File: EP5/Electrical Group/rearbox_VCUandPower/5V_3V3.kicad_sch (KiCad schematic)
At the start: 54 parts, among them IC2 LMR14050SDDAR, IC3 MCP6C04T-100E_CHY, IC4 LD39100PU33RY, J12 5V external, J13 USBC_RPI_5VOnly, J14 USBA_RPI_5Vonly, J15 fan1, J16 fan2, J17 UPS_cap, J18 5Vout, J19 Rpi, J21 3V3out

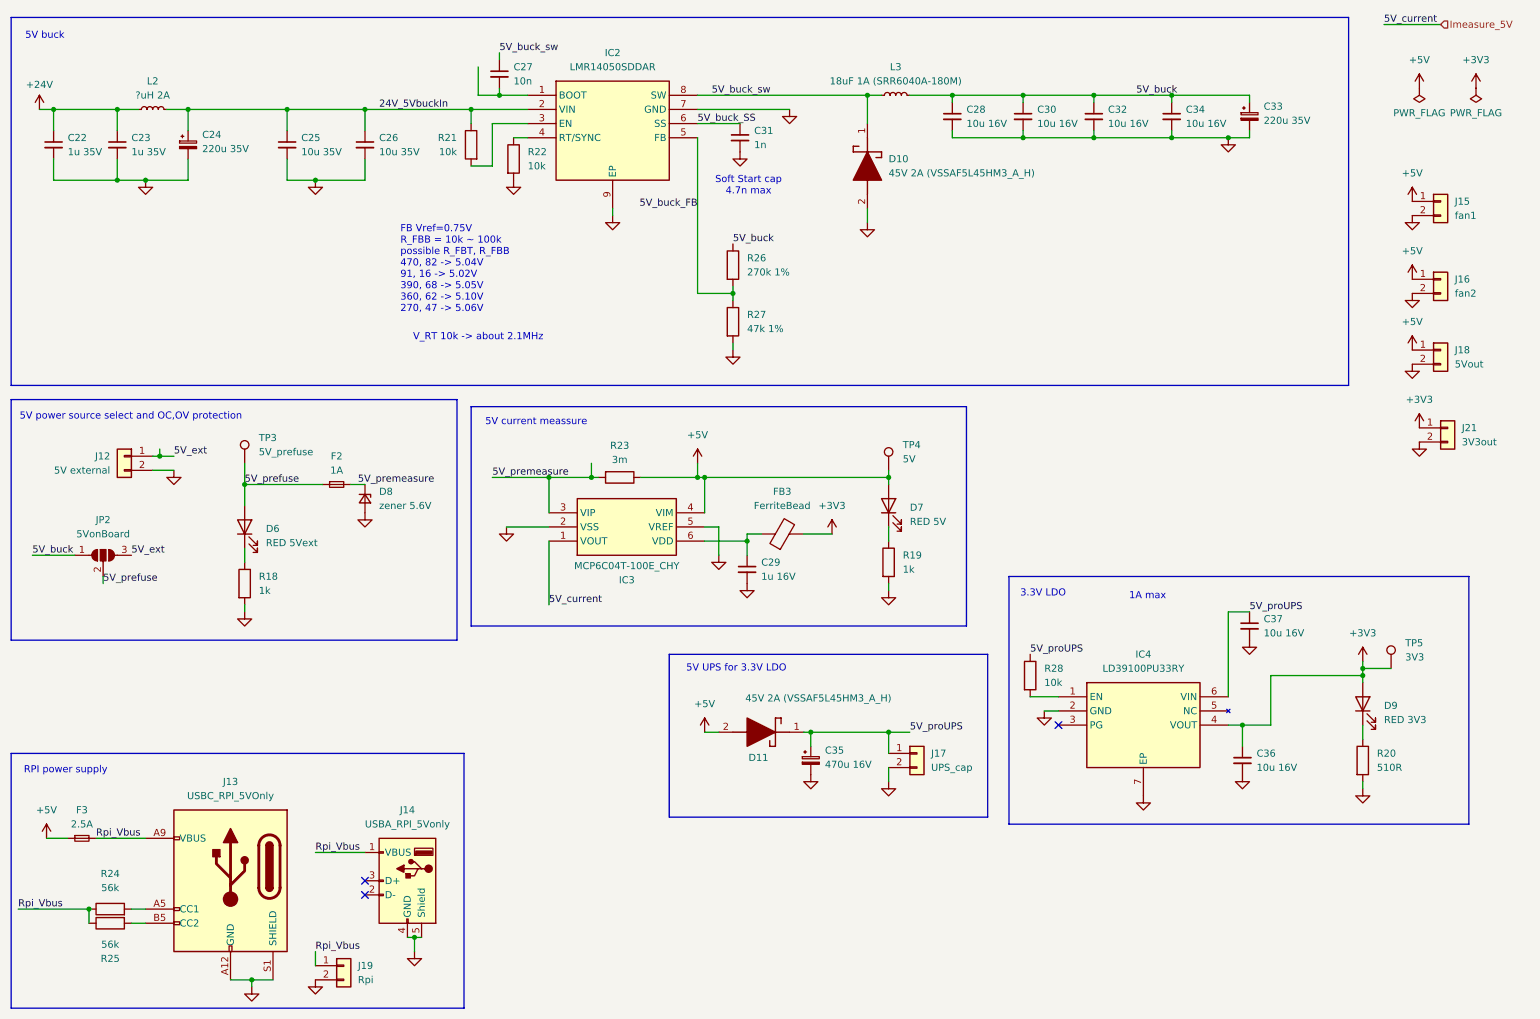
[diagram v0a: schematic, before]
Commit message: add rearbox_VCUandPower to EP5
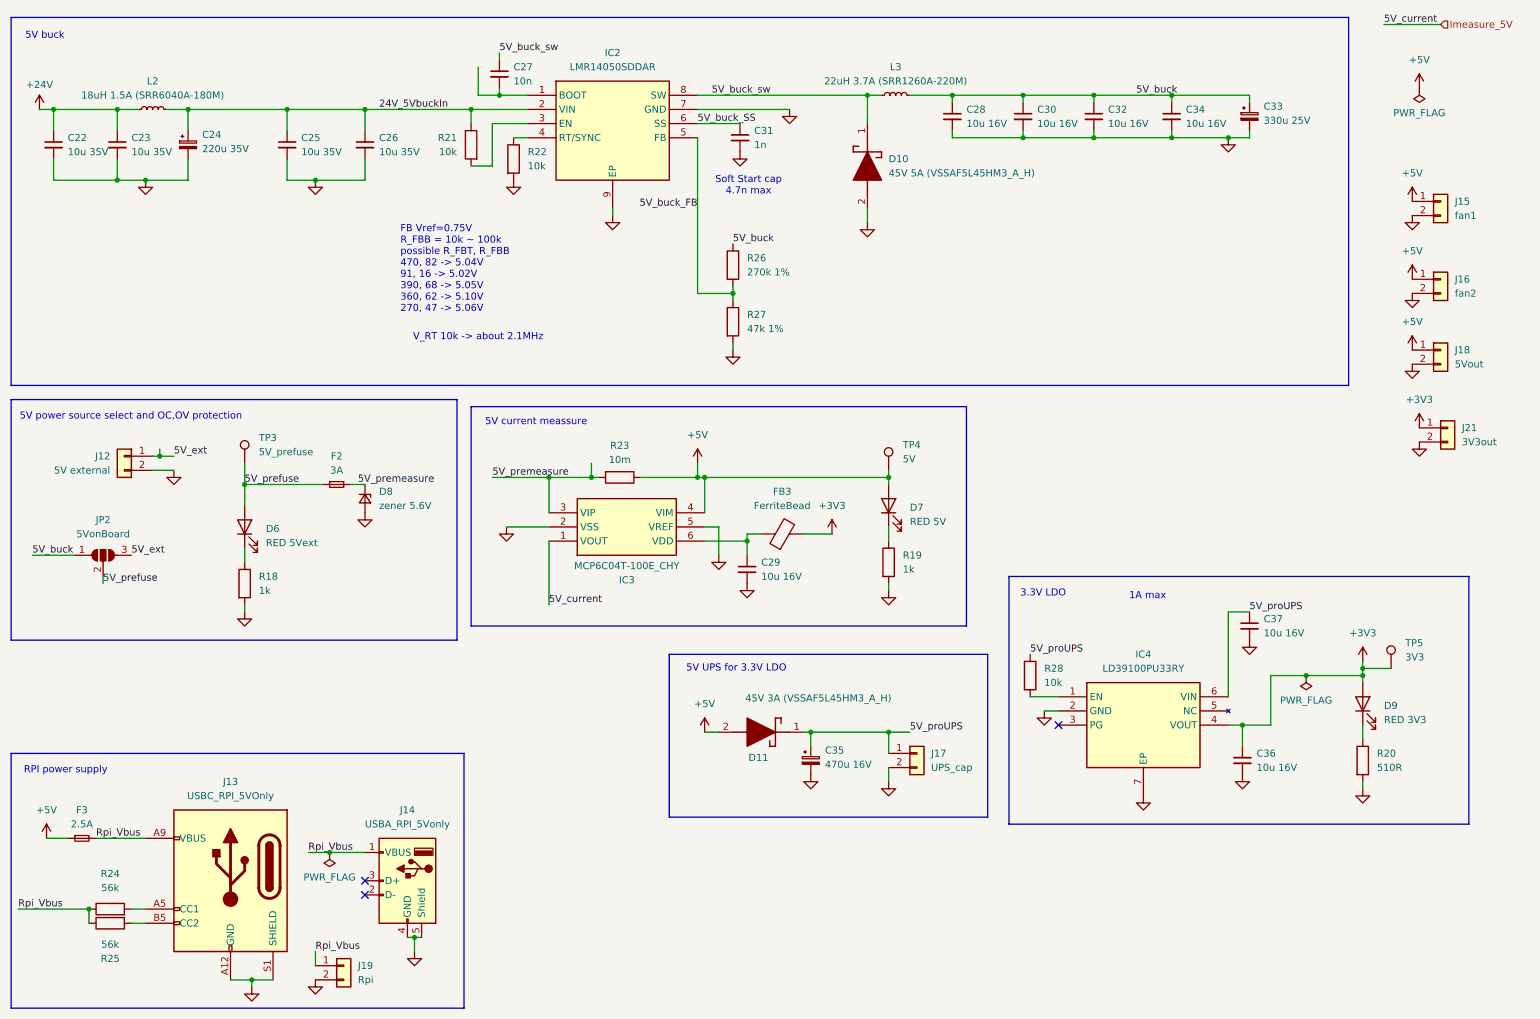
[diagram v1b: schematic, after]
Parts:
- C22, C23: value 1u 35V -> 10u 35V; footprint Capacitor_SMD:C_0805_2012Metric -> Capacitor_SMD:C_1206_3216Metric
- C29: value 1u 16V -> 10u 16V
- C33: value 220u 35V -> 330u 25V
- D10: value 45V 2A (VSSAF5L45HM3_A_H) -> 45V 5A (VSSAF5L45HM3_A_H)
- D11: value 45V 2A (VSSAF5L45HM3_A_H) -> 45V 3A (VSSAF5L45HM3_A_H)
- F2: value 1A -> 3A
- L2: value ?uH 2A -> 18uH 1.5A (SRR6040A-180M)
- L3: value 18uF 1A (SRR6040A-180M) -> 22uH 3.7A (SRR1260A-220M); footprint SamacSys_Parts:SRR6040A180M -> SamacSys_Parts:SRR1260A220M
- R23: value 3m -> 10m
